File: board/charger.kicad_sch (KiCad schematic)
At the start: 23 parts, among them Q1 Q_PNP_BCEC, Q2 Q_PNP_BCEC, U1 DS2711E+

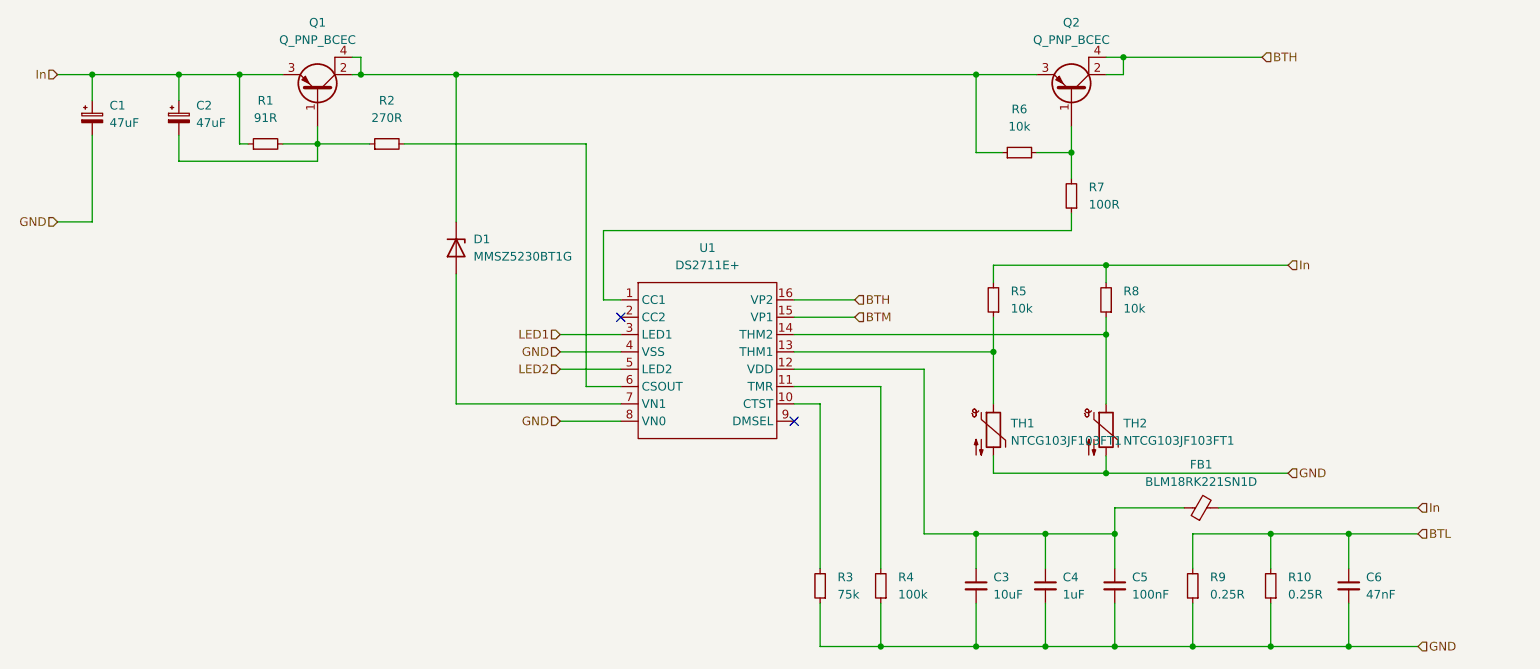
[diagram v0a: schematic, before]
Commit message: fixed missing connection
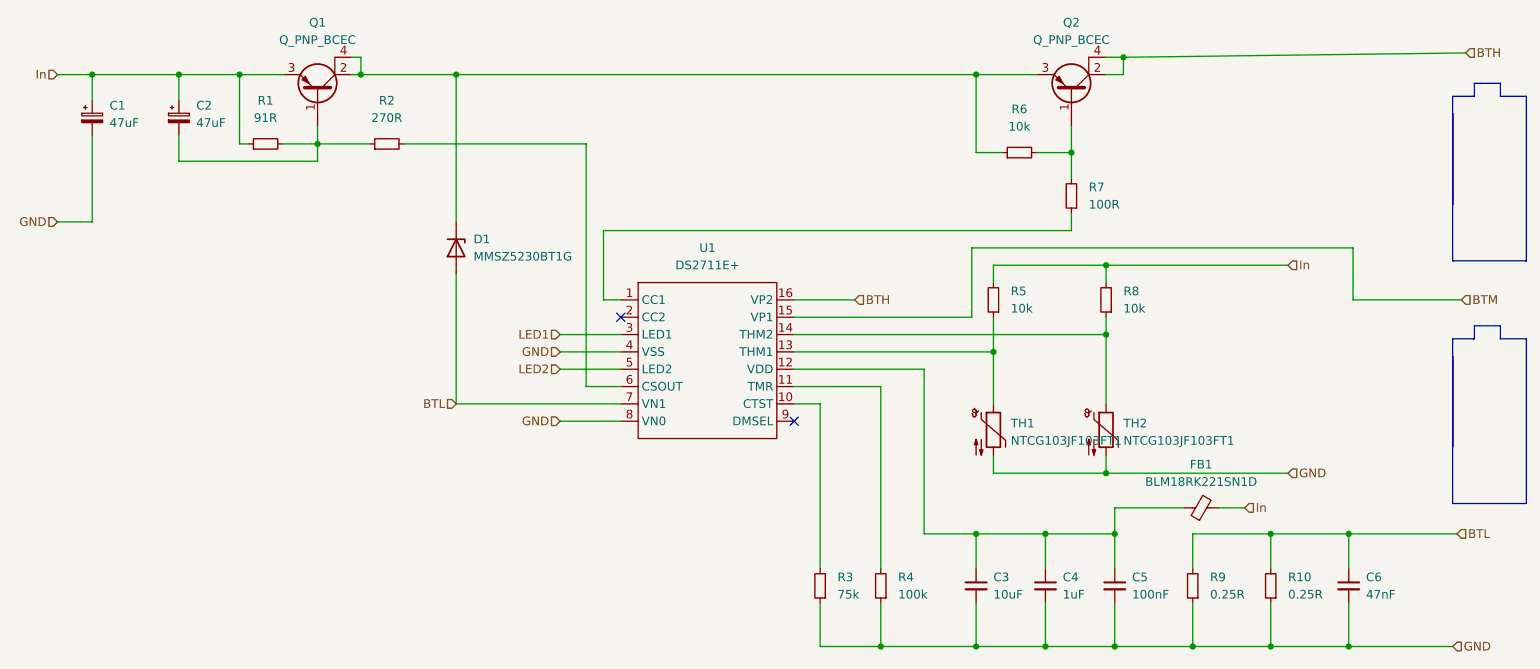
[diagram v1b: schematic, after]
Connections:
- net BTL: now also D1.2 (A), U1.7 (VN1)
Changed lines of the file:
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@@
+    (stroke (width 0) (type default) (color 0 0 0 0))
+  )
+  (polyline (pts (xy 241.935 52.705) (xy 241.935 50.8))
     (stroke (width 0) (type default) (color 0 0 0 0))
   )
@@
     (stroke (width 0) (type default) (color 0 0 0 0))
   )
+  (wire (pts (xy 220.345 82.55) (xy 220.345 74.93))
+    (stroke (width 0) (type default) (color 0 0 0 0))
+  )
   (wire (pts (xy 179.07 60.96) (xy 179.07 64.77))
     (stroke (width 0) (type default) (color 0 0 0 0))
@@
     (stroke (width 0) (type default) (color 0 0 0 0))
   )
-  (wire (pts (xy 207.01 46.99) (xy 186.69 46.99))
+  (polyline (pts (xy 238.125 88.265) (xy 234.95 88.265))
+    (stroke (width 0) (type default) (color 0 0 0 0))
+  )
+  (wire (pts (xy 236.855 46.355) (xy 186.69 46.99))
+    (stroke (width 0) (type default) (color 0 0 0 0))
+  )
+  (wire (pts (xy 236.22 82.55) (xy 220.345 82.55))
     (stroke (width 0) (type default) (color 0 0 0 0))
   )
@@
     (stroke (width 0) (type default) (color 0 0 0 0))
   )
+  (polyline (pts (xy 234.95 88.265) (xy 234.95 104.14))
+    (stroke (width 0) (type default) (color 0 0 0 0))
+  )
   (wire (pts (xy 74.93 46.99) (xy 74.93 49.53))
     (stroke (width 0) (type default) (color 0 0 0 0))
   )
+  (polyline (pts (xy 241.935 88.265) (xy 241.935 86.36))
+    (stroke (width 0) (type default) (color 0 0 0 0))
+  )
   (wire (pts (xy 208.28 127) (xy 208.28 133.35))
     (stroke (width 0) (type default) (color 0 0 0 0))
@@
     (stroke (width 0) (type default) (color 0 0 0 0))
   )
+  (wire (pts (xy 164.465 74.93) (xy 164.465 85.09))
+    (stroke (width 0) (type default) (color 0 0 0 0))
+  )
+  (polyline (pts (xy 241.935 86.36) (xy 238.125 86.36))
+    (stroke (width 0) (type default) (color 0 0 0 0))
+  )
   (wire (pts (xy 184.15 77.47) (xy 184.15 80.01))
     (stroke (width 0) (type default) (color 0 0 0 0))
   )
+  (polyline (pts (xy 245.745 88.265) (xy 241.935 88.265))
+    (stroke (width 0) (type default) (color 0 0 0 0))
+  )
   (wire (pts (xy 167.64 90.17) (xy 138.43 90.17))
     (stroke (width 0) (type default) (color 0 0 0 0))
@@
     (stroke (width 0) (type default) (color 0 0 0 0))
   )
-  (wire (pts (xy 200.66 113.03) (xy 229.87 113.03))
+  (wire (pts (xy 200.66 113.03) (xy 204.47 113.03))
+    (stroke (width 0) (type default) (color 0 0 0 0))
+  )
+  (polyline (pts (xy 234.95 90.805) (xy 234.95 112.395))
     (stroke (width 0) (type default) (color 0 0 0 0))
   )
@@
     (stroke (width 0) (type default) (color 0 0 0 0))
   )
+  (polyline (pts (xy 238.125 86.36) (xy 238.125 88.265))
+    (stroke (width 0) (type default) (color 0 0 0 0))
+  )
+  (polyline (pts (xy 234.95 76.835) (xy 245.745 76.835))
+    (stroke (width 0) (type default) (color 0 0 0 0))
+  )
   (wire (pts (xy 184.15 77.47) (xy 210.82 77.47))
     (stroke (width 0) (type default) (color 0 0 0 0))
   )
+  (polyline (pts (xy 234.95 55.245) (xy 234.95 76.835))
+    (stroke (width 0) (type default) (color 0 0 0 0))
+  )
+  (polyline (pts (xy 234.95 52.705) (xy 234.95 68.58))
+    (stroke (width 0) (type default) (color 0 0 0 0))
+  )
   (wire (pts (xy 185.42 133.35) (xy 175.26 133.35))
     (stroke (width 0) (type default) (color 0 0 0 0))
@@
     (stroke (width 0) (type default) (color 0 0 0 0))
   )
+  (polyline (pts (xy 238.125 50.8) (xy 238.125 52.705))
+    (stroke (width 0) (type default) (color 0 0 0 0))
+  )
   (wire (pts (xy 196.85 121.92) (xy 196.85 116.84))
     (stroke (width 0) (type default) (color 0 0 0 0))
@@
     (stroke (width 0) (type default) (color 0 0 0 0))
   )
+  (polyline (pts (xy 245.745 112.395) (xy 245.745 88.265))
+    (stroke (width 0) (type default) (color 0 0 0 0))
+  )
   (wire (pts (xy 151.13 95.25) (xy 138.43 95.25))
     (stroke (width 0) (type default) (color 0 0 0 0))
   )
-  (wire (pts (xy 219.71 116.84) (xy 229.87 116.84))
+  (wire (pts (xy 219.71 116.84) (xy 235.585 116.84))
     (stroke (width 0) (type default) (color 0 0 0 0))
   )
@@
     (stroke (width 0) (type default) (color 0 0 0 0))
   )
+  (polyline (pts (xy 234.95 112.395) (xy 245.745 112.395))
+    (stroke (width 0) (type default) (color 0 0 0 0))
+  )
   (wire (pts (xy 219.71 133.35) (xy 208.28 133.35))
     (stroke (width 0) (type default) (color 0 0 0 0))
@@
     (stroke (width 0) (type default) (color 0 0 0 0))
   )
+  (polyline (pts (xy 238.125 52.705) (xy 234.95 52.705))
+    (stroke (width 0) (type default) (color 0 0 0 0))
+  )
   (wire (pts (xy 167.64 97.79) (xy 167.64 90.17))
     (stroke (width 0) (type default) (color 0 0 0 0))
@@
     (stroke (width 0) (type default) (color 0 0 0 0))
   )
-  (wire (pts (xy 138.43 85.09) (xy 147.32 85.09))
+  (wire (pts (xy 138.43 85.09) (xy 164.465 85.09))
     (stroke (width 0) (type default) (color 0 0 0 0))
   )
@@
     (stroke (width 0) (type default) (color 0 0 0 0))
   )
-  (wire (pts (xy 229.87 133.35) (xy 219.71 133.35))
+  (wire (pts (xy 234.95 133.35) (xy 219.71 133.35))
     (stroke (width 0) (type default) (color 0 0 0 0))
   )
@@
     (stroke (width 0) (type default) (color 0 0 0 0))
   )
+  (polyline (pts (xy 245.745 76.835) (xy 245.745 52.705))
+    (stroke (width 0) (type default) (color 0 0 0 0))
+  )
+  (wire (pts (xy 220.345 74.93) (xy 164.465 74.93))
+    (stroke (width 0) (type default) (color 0 0 0 0))
+  )
   (wire (pts (xy 165.1 60.96) (xy 165.1 49.53))
     (stroke (width 0) (type default) (color 0 0 0 0))
   )
+  (polyline (pts (xy 241.935 50.8) (xy 238.125 50.8))
+    (stroke (width 0) (type default) (color 0 0 0 0))
+  )
   (wire (pts (xy 175.26 121.92) (xy 175.26 116.84))
     (stroke (width 0) (type default) (color 0 0 0 0))
@@
     (stroke (width 0) (type default) (color 0 0 0 0))
   )
+  (polyline (pts (xy 245.745 52.705) (xy 241.935 52.705))
+    (stroke (width 0) (type default) (color 0 0 0 0))
+  )
   (wire (pts (xy 88.9 97.79) (xy 113.03 97.79))
     (stroke (width 0) (type default) (color 0 0 0 0))
@@
     (stroke (width 0) (type default) (color 0 0 0 0))
   )
-  (hierarchical_label "BTL" (shape input) (at 229.87 116.84 0)
+  (hierarchical_label "BTL" (shape input) (at 235.585 116.84 0)
     (effects (font (size 1.27 1.27)) (justify left))
   )
@@
     (effects (font (size 1.27 1.27)) (justify left))
   )
-  (hierarchical_label "GND" (shape input) (at 229.87 133.35 0)
+  (hierarchical_label "GND" (shape input) (at 234.95 133.35 0)
     (effects (font (size 1.27 1.27)) (justify left))
   )
@@
     (effects (font (size 1.27 1.27)) (justify left))
   )
-  (hierarchical_label "In" (shape input) (at 229.87 113.03 0)
-    (effects (font (size 1.27 1.27)) (justify left))
-  )
-  (hierarchical_label "BTH" (shape input) (at 207.01 46.99 0)
-    (effects (font (size 1.27 1.27)) (justify left))
-  )
-  (hierarchical_label "BTM" (shape input) (at 147.32 85.09 0)
-    (effects (font (size 1.27 1.27)) (justify left))
-  )
+  (hierarchical_label "BTL" (shape input) (at 88.9 97.79 180)
+    (effects (font (size 1.27 1.27)) (justify right))
+  )
+  (hierarchical_label "In" (shape input) (at 204.47 113.03 0)
+    (effects (font (size 1.27 1.27)) (justify left))
+  )
+  (hierarchical_label "BTH" (shape input) (at 236.855 46.355 0)
+    (effects (font (size 1.27 1.27)) (justify left))
+  )
+  (hierarchical_label "BTM" (shape input) (at 236.22 82.55 0)
+    (effects (font (size 1.27 1.27)) (justify left))
+  )

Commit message: fixed footprint
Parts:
- U1: footprint Package_SO:TSSOP-16_4.4x3.6mm_P0.4mm -> b105:SOP65P640X110-16N
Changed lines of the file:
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@@
     (property "Reference" "U1" (id 0) (at 125.73 74.93 0))
     (property "Value" "DS2711E+" (id 1) (at 125.73 77.47 0))
-    (property "Footprint" "Package_SO:TSSOP-16_4.4x3.6mm_P0.4mm" (id 2) (at 125.73 81.28 0)
+    (property "Footprint" "b105:SOP65P640X110-16N" (id 2) (at 125.73 81.28 0)
       (effects (font (size 1.27 1.27)) hide)
     )

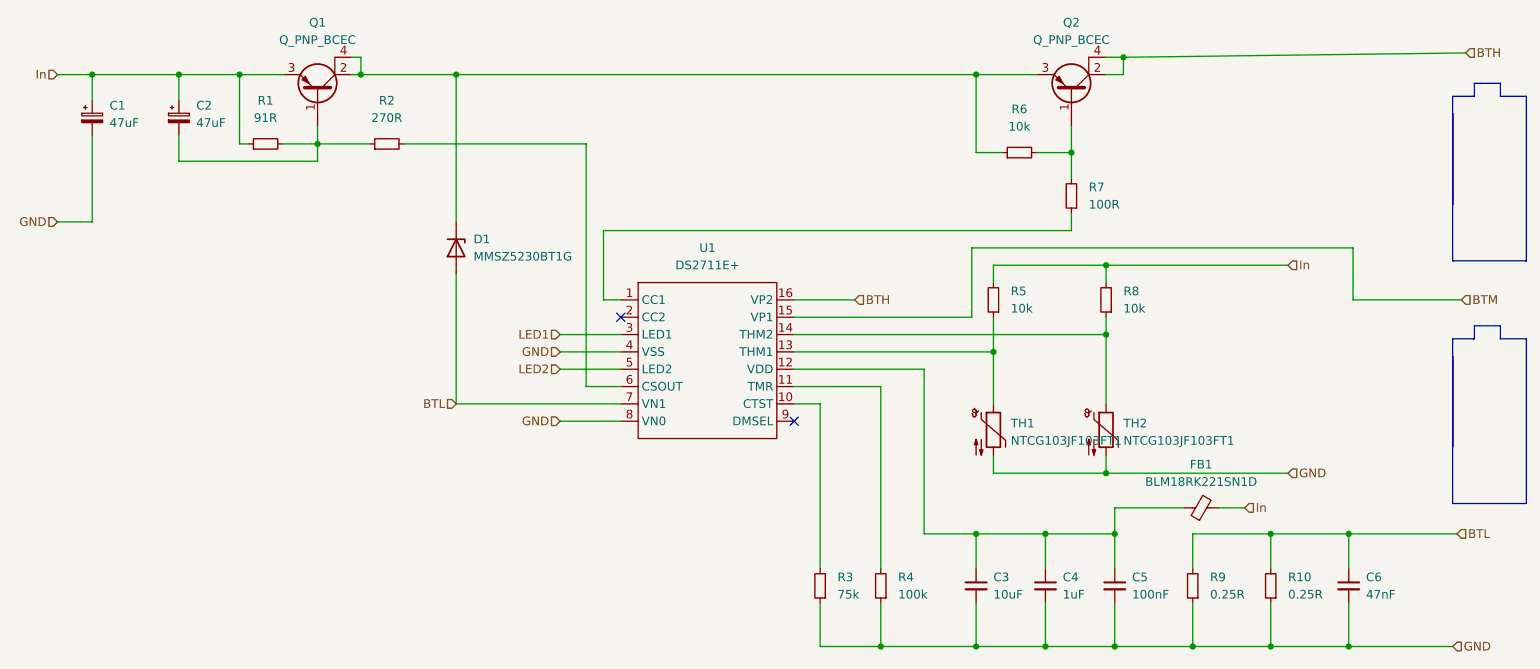
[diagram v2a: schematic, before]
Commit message: added missing limmiting resistor to protect zener diode
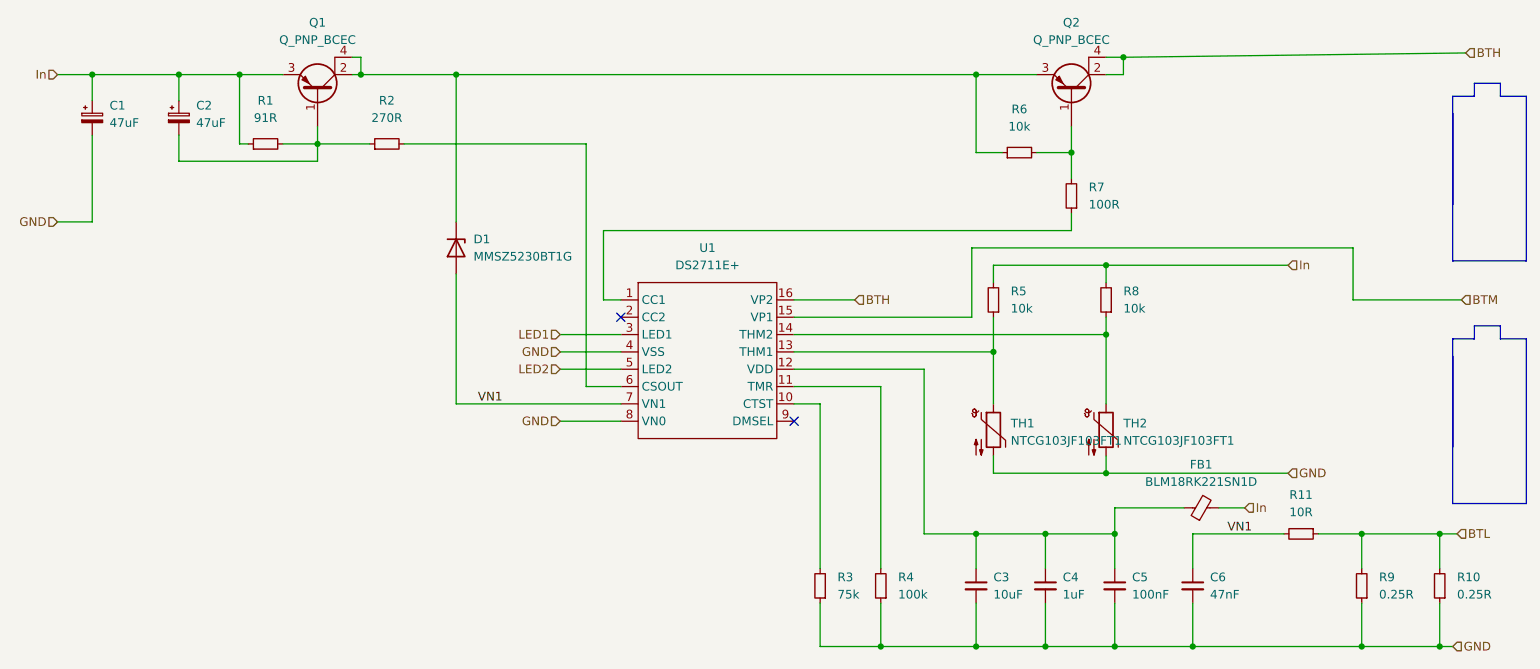
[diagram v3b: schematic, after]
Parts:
- added R11: 10R, Resistor_SMD:R_0603_1608Metric, symbol Device:R_Small
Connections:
- net BTL: now also R11.1; no longer C6.1, D1.2 (A), U1.7 (VN1)
- new net VN1: C6.1, D1.2 (A), R11.2, U1.7 (VN1)
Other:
- moved on the sheet: C6, R10, R9
